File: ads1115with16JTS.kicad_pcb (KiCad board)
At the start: 2 copper layers, 45.7 x 68.6 mm, 50 parts, among them J1 Conn_01x02_Pin, J10 Conn_01x02_Pin, J11 Conn_01x02_Pin, J12 Conn_01x02_Pin, J13 Conn_01x02_Pin, J14 Conn_01x02_Pin, J15 Conn_01x02_Pin, J16 Conn_01x02_Pin, J17 Conn_01x04_Pin, J18 PinSocket_1x20_P2.54mm_Vertic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, J19 PinSocket_1x20_P2.54mm_Vertic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, J2 Conn_01x02_Pin, J20 Screw_Terminal_01x02, J3 Conn_01x02_Pin, J4 Conn_01x02_Pin, J5 Conn_01x02_Pin, J6 Conn_01x02_Pin, J7 Conn_01x02_Pin, J8 Conn_01x02_Pin, J9 Conn_01x02_Pin, U1 ADS1115IDGS, U2 ADS1115IDGS, U3 ADS1115IDGS, U4 ADS1115IDGS

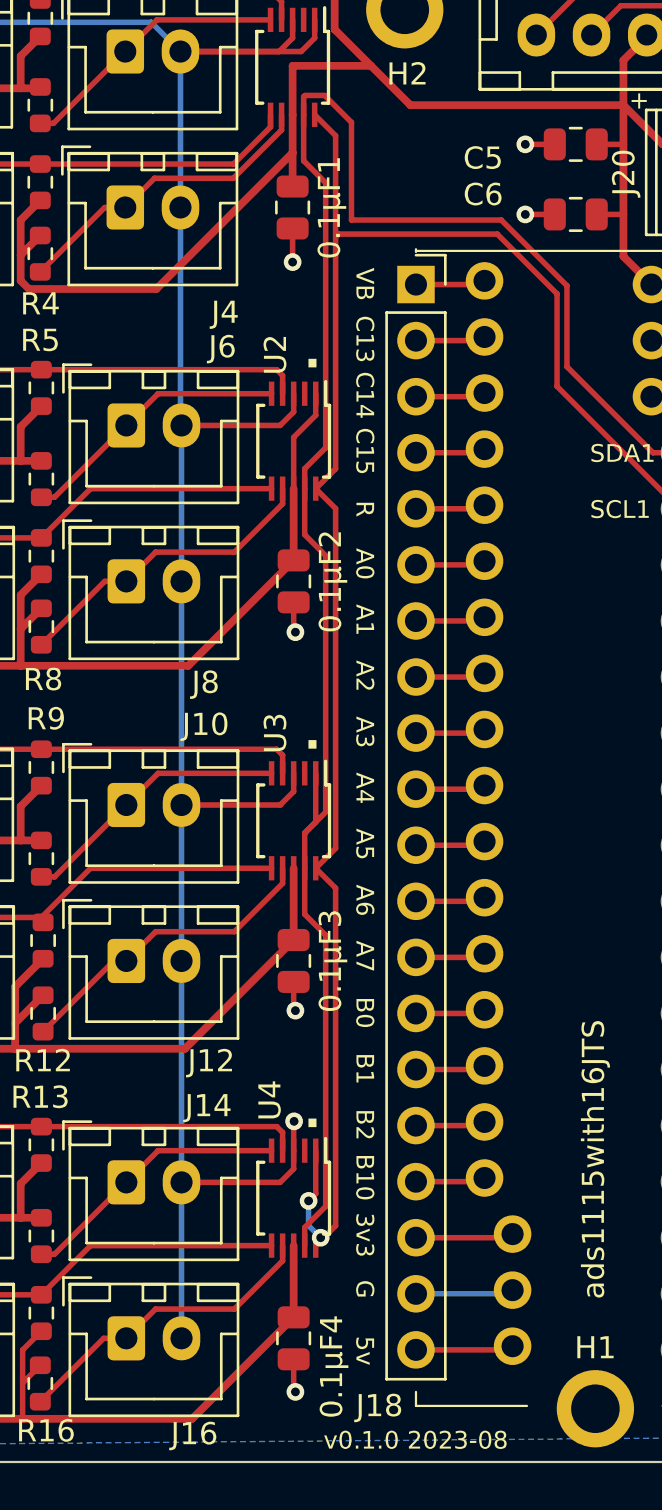
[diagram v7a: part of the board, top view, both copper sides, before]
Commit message: footprint lib adjustments.
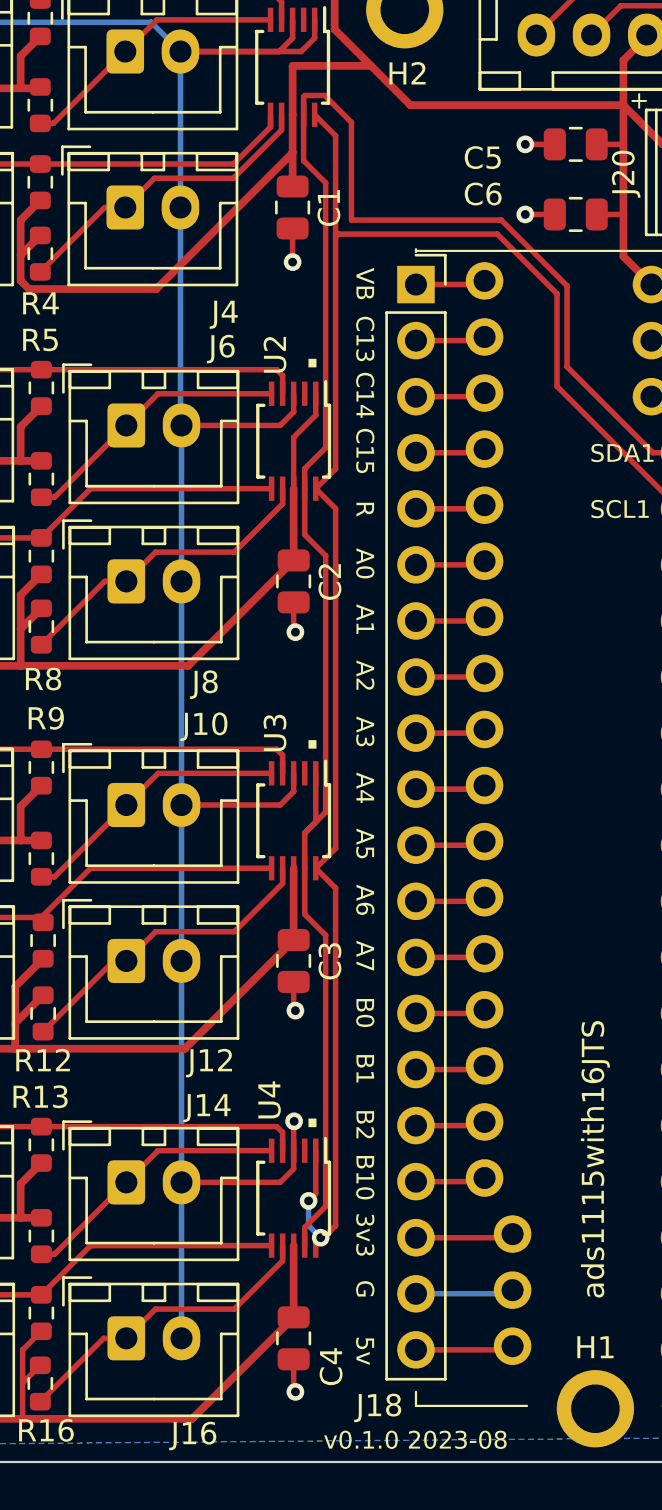
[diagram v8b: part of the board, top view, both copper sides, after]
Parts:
- C1: renamed from 0.1µF1; value C1 -> 0.1µF1; footprint Capacitor_SMD:C_0805_2012Metric -> ProjectLib:C_0805_2012Metric
- C2: renamed from 0.1µF2; value C2 -> 0.1µF1; footprint Capacitor_SMD:C_0805_2012Metric -> ProjectLib:C_0805_2012Metric
- C3: renamed from 0.1µF3; value C3 -> 0.1µF1; footprint Capacitor_SMD:C_0805_2012Metric -> ProjectLib:C_0805_2012Metric
- C4: renamed from 0.1µF4; value C4 -> 0.1µF1; footprint Capacitor_SMD:C_0805_2012Metric -> ProjectLib:C_0805_2012Metric
- C5, C6: footprint Capacitor_SMD:C_0805_2012Metric -> ProjectLib:C_0805_2012Metric
- H1, H2: footprint MountingHole:MountingHole_2.2mm_M2_ISO7380_Pad -> ProjectLib:MountingHole_2.2mm_M2_ISO7380_Pad
- J**1: footprint PG:b_pill_takeoffPads_1-20 -> ProjectLib:b_pill_takeoffPads_1-20
- J**2: footprint PG:b_pill_takeoffPads_21-40 -> ProjectLib:b_pill_takeoffPads_21-40
- J1, J10, J11, J12, J13, J14, J15, J16, J2, J3, J4, J5, J6, J7, J8, J9: footprint Connector_JST:JST_XH_B2B-XH-A_1x02_P2.50mm_Vertical -> ProjectLib:JST_XH_B2B-XH-A_1x02_P2.50mm_Vertical
- J17: footprint Connector_JST:JST_XH_B4B-XH-A_1x04_P2.50mm_Vertical -> ProjectLib:JST_XH_B4B-XH-A_1x04_P2.50mm_Vertical
- J18: footprint PG:b_pill_socket_1-20 -> ProjectLib:b_pill_socket_1-20
- J19: footprint PG:b_pill_socket_21-40 -> ProjectLib:b_pill_socket_21-40
- J20: footprint TerminalBlock_Phoenix:TerminalBlock_Phoenix_MPT-0,5-2-2.54_1x02_P2.54mm_Horizontal -> ProjectLib:TerminalBlock_Phoenix_MPT-0,5-2-2.54_1x02_P2.54mm_Horizontal
- R1, R10, R11, R12, R13, R14, R15, R16, R2, R3, R4, R5, R6, R7, R8, R9: footprint Resistor_SMD:R_0603_1608Metric -> ProjectLib:R_0603_1608Metric
- U1, U2, U3, U4: footprint Package_SO:TSSOP-10_3x3mm_P0.5mm -> ProjectLib:TSSOP-10_3x3mm_P0.5mm
